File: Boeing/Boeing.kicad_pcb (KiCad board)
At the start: 2 copper layers, 75 x 25 mm, 1 part

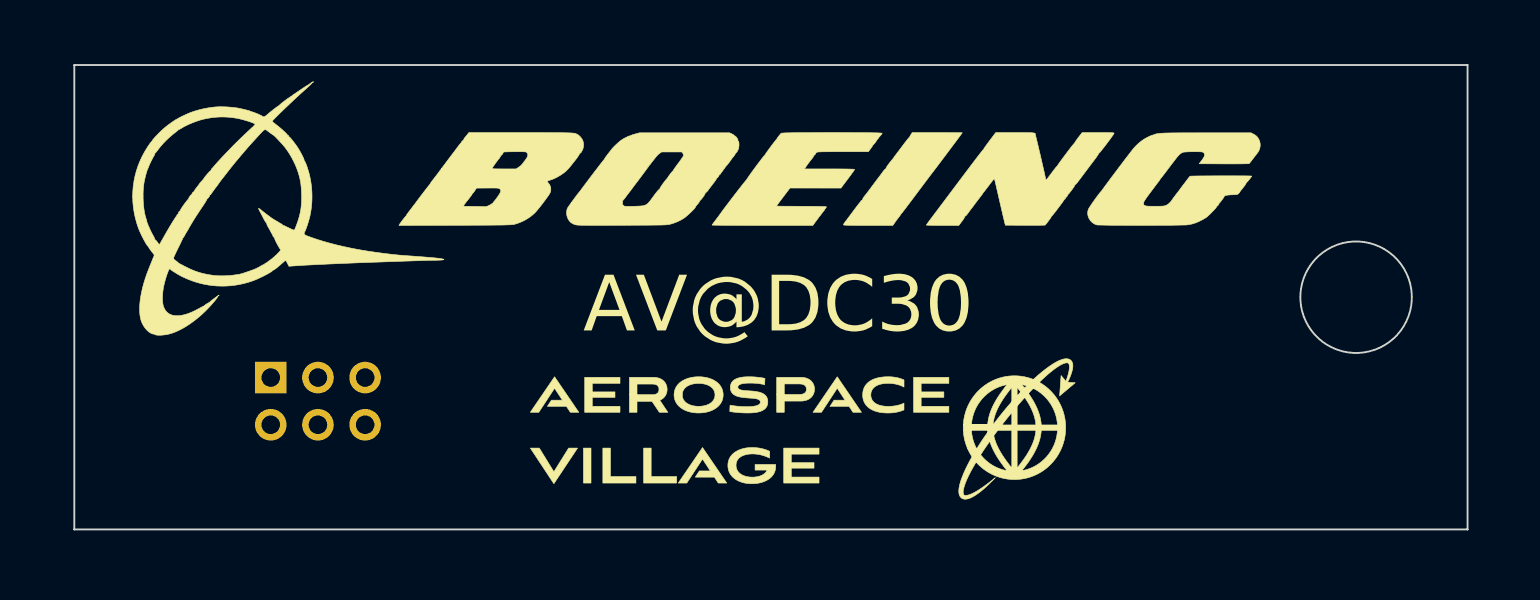
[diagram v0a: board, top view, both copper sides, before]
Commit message: Boeing SAO update to give their logo more space
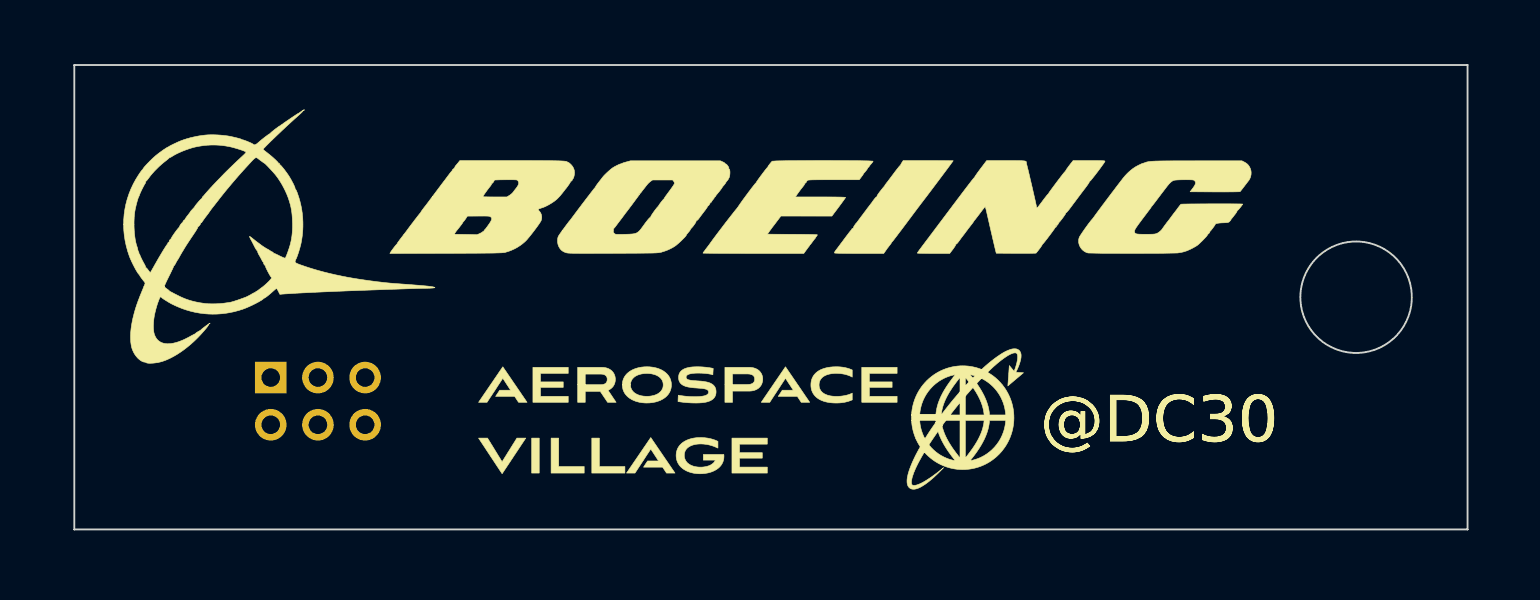
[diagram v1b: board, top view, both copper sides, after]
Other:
- board text added: "@DC30"
- board text removed: "AV@DC30"

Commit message: updated the Boeing SAO to reflect their logo guidelines and added an LED
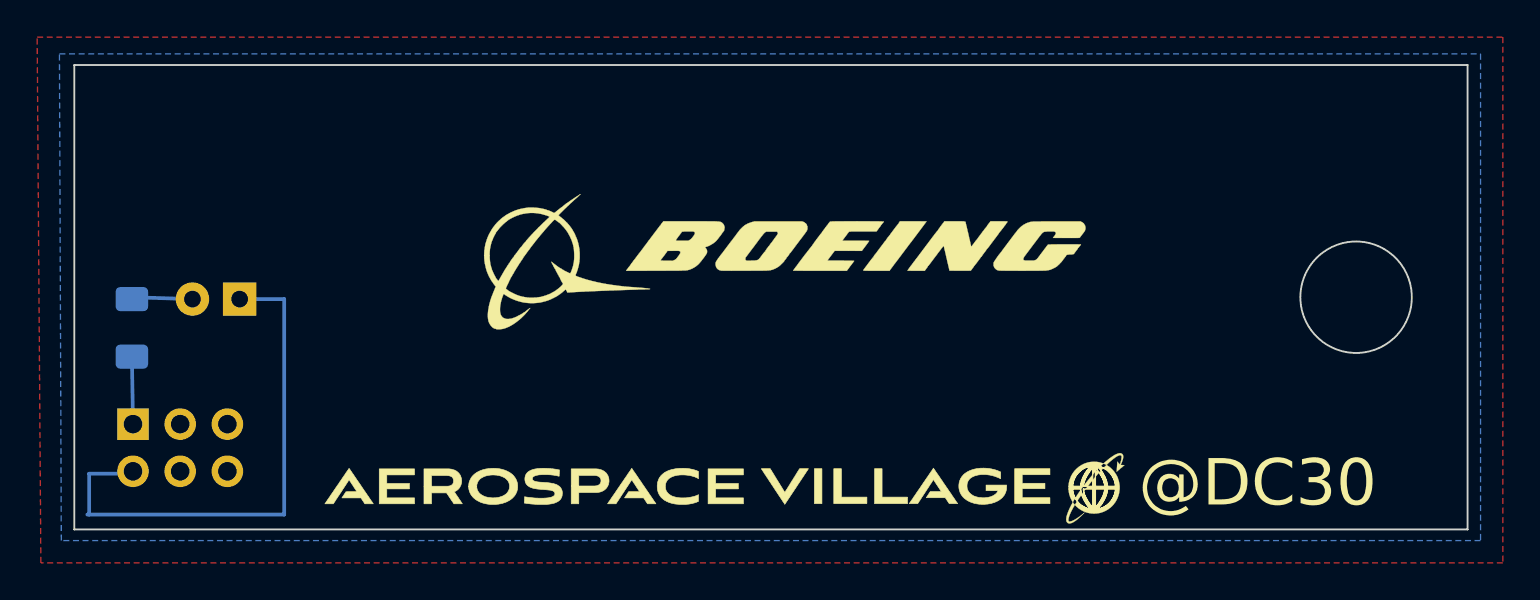
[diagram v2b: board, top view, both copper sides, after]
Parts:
- added REF**: LED_D5.0mm, LED_THT:LED_D5.0mm, F.Cu at (108.9, 62.6)
- added REF**: R_1206_3216Metric_Pad1.30x1.75mm_HandSolder, Resistor_SMD:R_1206_3216Metric_Pad1.30x1.75mm_HandSolder, B.Cu at (103.1, 64.2)
- moved REF** 7.83 mm to (103.2, 69.3)
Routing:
- added copper zone on B.Cu, net (none)
- added copper zone on F.Cu, net (none)
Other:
- board text added: "v3"
- board text removed: "v1"

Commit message: v3 of Boeing SAO
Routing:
- net (no net): track 0.00 -> 32.2 mm
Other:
- board text added: "@av_pubs v3"
- board text removed: "v3"
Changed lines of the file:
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@@
   )
   (setup
+    (stackup
+      (layer "F.SilkS" (type "Top Silk Screen"))
+      (layer "F.Paste" (type "Top Solder Paste"))
+      (layer "F.Mask" (type "Top Solder Mask") (thickness 0.01))
+      (layer "F.Cu" (type "copper") (thickness 0.035))
+      (layer "dielectric 1" (type "core") (thickness 1.51) (material "FR4") (epsilon_r 4.5) (loss_tangent 0.02))
+      (layer "B.Cu" (type "copper") (thickness 0.035))
+      (layer "B.Mask" (type "Bottom Solder Mask") (thickness 0.01))
+      (layer "B.Paste" (type "Bottom Solder Paste"))
+      (layer "B.SilkS" (type "Bottom Silk Screen"))
+      (copper_finish "None")
+      (dielectric_constraints no)
+    )
     (pad_to_mask_clearance 0)
     (pcbplotparams
@@
       (plot_on_all_layers_selection 0x0000000_00000000)
       (disableapertmacros false)
-      (usegerberextensions true)
-      (usegerberattributes true)
+      (usegerberextensions false)
+      (usegerberattributes false)
       (usegerberadvancedattributes false)
       (creategerberjobfile false)
@@
     )
   )
-  (gr_line (start 111.3 74.2) (end 111.3 62.6)
-    (stroke (width 0.2) (type default)) (layer "B.Cu"))
-  (gr_line (start 100.8 72) (end 100.8 74.2)
-    (stroke (width 0.2) (type default)) (layer "B.Cu"))
-  (gr_line (start 103.1 65.7) (end 103.16 69.33)
-    (stroke (width 0.2) (type default)) (layer "B.Cu"))
-  (gr_line (start 100.7 74.2) (end 111.3 74.2)
-    (stroke (width 0.2) (type default)) (layer "B.Cu"))
-  (gr_line (start 111.3 62.6) (end 108.9 62.6)
-    (stroke (width 0.2) (type default)) (layer "B.Cu"))
-  (gr_line (start 100.8 72) (end 103.1 72)
-    (stroke (width 0.2) (type default)) (layer "B.Cu"))
-  (gr_line (start 103.1 62.5) (end 106.3 62.6)
-    (stroke (width 0.2) (type default)) (layer "B.Cu"))
   (gr_line (start 153.74701 72.576395) (end 153.740758 72.626782)
     (stroke (width 0.019843) (type solid)) (layer "F.SilkS"))
@@
   (gr_circle (center 169 62.5) (end 172 62.5)
     (stroke (width 0.1) (type default)) (fill none) (layer "Edge.Cuts"))
-  (gr_text "v3" (at 173.6 74) (layer "B.SilkS")
-    (effects (font (size 1 1) (thickness 0.15)) (justify mirror))
+  (gr_text "@av_pubs\nv3" (at 174.2 55) (layer "B.Cu")
+    (effects (font (size 1.5 1.5) (thickness 0.3) bold) (justify left bottom mirror))
   )
   (gr_text "jlcjlcjlcjlc" (at 173.5 62.6 90) (layer "B.SilkS")
@@
     )
   )
+  (segment (start 103.1 74.2) (end 103.16 74.14) (width 0.254) (layer "B.Cu") (net 0))
+  (segment (start 103.2 74.3) (end 103.1 74.2) (width 0.254) (layer "B.Cu") (net 0))
+  (segment (start 103.16 74.14) (end 103.16 71.87) (width 0.254) (layer "B.Cu") (net 0))
+  (segment (start 113.6 67.3) (end 113.6 72.2) (width 0.254) (layer "B.Cu") (net 0))
+  (segment (start 113.6 72.2) (end 111.5 74.3) (width 0.254) (layer "B.Cu") (net 0))
+  (segment (start 106.36 62.6) (end 103.1 62.6) (width 0.254) (layer "B.Cu") (net 0))
+  (segment (start 103.16 65.76) (end 103.16 69.33) (width 0.254) (layer "B.Cu") (net 0))
+  (segment (start 103.1 65.7) (end 103.16 65.76) (width 0.254) (layer "B.Cu") (net 0))
+  (segment (start 108.9 62.6) (end 113.6 67.3) (width 0.254) (layer "B.Cu") (net 0))
+  (segment (start 111.5 74.3) (end 103.2 74.3) (width 0.254) (layer "B.Cu") (net 0))
   (zone (net 0) (net_name "") (layer "F.Cu") (hatch edge 0.508)
     (connect_pads (clearance 0.508))

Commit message: v4 of Boeing SAO
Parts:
- removed REF**: LED_D5.0mm, LED_THT:LED_D5.0mm
- removed REF**: PinHeader_2x03_P2.54mm_Vertical, Connector_PinHeader_2.54mm:PinHeader_2x03_P2.54mm_Vertical
- removed REF**: R_1206_3216Metric_Pad1.30x1.75mm_HandSolder, Resistor_SMD:R_1206_3216Metric_Pad1.30x1.75mm_HandSolder
- added D1: LED, LED_THT:LED_D5.0mm, F.Cu at (108.9, 62.6)
- added J1: Conn_02x03_Counter_Clockwise, Connector_PinHeader_2.54mm:PinHeader_2x03_P2.54mm_Vertical, B.Cu at (103.2, 69.3)
- added R1: R, Resistor_SMD:R_1206_3216Metric_Pad1.30x1.75mm_HandSolder, B.Cu at (101.7, 62.5)
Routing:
- net (no net): track 32.2 -> 0.00 mm
- net Net-(D1-K): track 0.00 -> 24.1 mm
- net Net-(J1-Pin_1): track 0.00 -> 5.88 mm
- net Net-(D1-A): track 0.00 -> 5.34 mm
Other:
- outline, holes or cut-outs redrawn
- board text added: "@av_pubs v4"
- board text removed: "@av_pubs v3"
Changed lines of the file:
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@@
   )
   (net 0 "")
+  (net 1 "Net-(D1-K)")
+  (net 2 "Net-(D1-A)")
+  (net 3 "Net-(J1-Pin_1)")
+  (net 4 "unconnected-(J1-Pin_3)")
+  (net 5 "unconnected-(J1-Pin_4)")
+  (net 6 "unconnected-(J1-Pin_5)")
+  (net 7 "unconnected-(J1-Pin_6)")
   (footprint "LED_THT:LED_D5.0mm" (layer "F.Cu")
     (at 108.9 62.6 180)
     (descr "LED, diameter 5.0mm, 2 pins, http://cdn-reichelt.de/documents/datenblatt/A500/LL-504BC2E-009.pdf")
     (tags "LED diameter 5.0mm 2 pins")
+    (property "Sheetfile" "File: Boeing.kicad_sch")
+    (property "Sheetname" "")
+    (property "ki_description" "Light emitting diode")
+    (property "ki_keywords" "LED diode")
     (attr through_hole)
-    (fp_text reference "REF**" (at 1.27 -3.96) (layer "F.SilkS") hide
+    (fp_text reference "D1" (at 1.27 -3.96) (layer "F.SilkS") hide
         (effects (font (size 1 1) (thickness 0.15)))
     )
-    (fp_text value "LED_D5.0mm" (at 1.27 3.96) (layer "F.Fab")
+    (fp_text value "LED" (at 1.27 3.96) (layer "F.Fab")
         (effects (font (size 1 1) (thickness 0.15)))
     )
@@
         (effects (font (size 0.8 0.8) (thickness 0.2)))
     )
+    (fp_line (start -1.29 -1.545) (end -1.29 1.545)
+      (stroke (width 0.12) (type solid)) (layer "F.SilkS"))
+    (fp_arc (start -1.29 -1.54483) (mid 2.072002 -2.880433) (end 4.26 0.000462)
+      (stroke (width 0.12) (type solid)) (layer "F.SilkS"))
+    (fp_arc (start 4.26 -0.000462) (mid 2.072002 2.880433) (end -1.29 1.54483)
+      (stroke (width 0.12) (type solid)) (layer "F.SilkS"))
+    (fp_circle (center 1.27 0) (end 3.77 0)
+      (stroke (width 0.12) (type solid)) (fill none) (layer "F.SilkS"))
     (fp_line (start -1.95 -3.25) (end -1.95 3.25)
       (stroke (width 0.05) (type solid)) (layer "F.CrtYd"))
@@
     (fp_circle (center 1.27 0) (end 3.77 0)
       (stroke (width 0.1) (type solid)) (fill none) (layer "F.Fab"))
-    (pad "1" thru_hole rect (at 0 0 180) (size 1.8 1.8) (drill 0.9) (layers *.Cu *.Mask))
-    (pad "2" thru_hole circle (at 2.54 0 180) (size 1.8 1.8) (drill 0.9) (layers *.Cu *.Mask))
+    (pad "1" thru_hole rect (at 0 0 180) (size 1.8 1.8) (drill 0.9) (layers *.Cu *.Mask)
+      (net 1 "Net-(D1-K)") (pinfunction "K") (pintype "passive"))
+    (pad "2" thru_hole circle (at 2.54 0 180) (size 1.8 1.8) (drill 0.9) (layers *.Cu *.Mask)
+      (net 2 "Net-(D1-A)") (pinfunction "A") (pintype "passive"))
     (model "${KICAD6_3DMODEL_DIR}/LED_THT.3dshapes/LED_D5.0mm.wrl"
       (offset (xyz 0 0 0))
@@
     (descr "Through hole straight pin header, 2x03, 2.54mm pitch, double rows")
     (tags "Through hole pin header THT 2x03 2.54mm double row")
+    (property "Sheetfile" "File: Boeing.kicad_sch")
+    (property "Sheetname" "")
+    (property "ki_description" "Generic connector, double row, 02x03, counter clockwise pin numbering scheme (similar to DIP packge numbering), script generated (kicad-library-utils/schlib/autogen/connector/)")
+    (property "ki_keywords" "connector")
     (attr through_hole)
-    (fp_text reference "REF**" (at 1.27 2.33 90) (layer "B.SilkS") hide
+    (fp_text reference "J1" (at 1.27 2.33 90) (layer "B.SilkS") hide
         (effects (font (size 1 1) (thickness 0.15)) (justify mirror))
     )
-    (fp_text value "PinHeader_2x03_P2.54mm_Vertical" (at 5.17 -0.14 -180) (layer "B.Fab")
+    (fp_text value "Conn_02x03_Counter_Clockwise" (at 1.27 -7.41 90) (layer "B.Fab")
         (effects (font (size 1 1) (thickness 0.15)) (justify mirror))
     )
@@
     (fp_line (start 3.81 1.27) (end 3.81 -6.35)
       (stroke (width 0.1) (type solid)) (layer "B.Fab"))
-    (pad "1" thru_hole rect (at 0 0 270) (size 1.7 1.7) (drill 1) (layers *.Cu *.Mask))
-    (pad "2" thru_hole oval (at 2.54 0 270) (size 1.7 1.7) (drill 1) (layers *.Cu *.Mask))
-    (pad "3" thru_hole oval (at 0 -2.54 270) (size 1.7 1.7) (drill 1) (layers *.Cu *.Mask))
-    (pad "4" thru_hole oval (at 2.54 -2.54 270) (size 1.7 1.7) (drill 1) (layers *.Cu *.Mask))
-    (pad "5" thru_hole oval (at 0 -5.08 270) (size 1.7 1.7) (drill 1) (layers *.Cu *.Mask))
-    (pad "6" thru_hole oval (at 2.54 -5.08 270) (size 1.7 1.7) (drill 1) (layers *.Cu *.Mask))
+    (pad "1" thru_hole rect (at 0 0 270) (size 1.7 1.7) (drill 1) (layers *.Cu *.Mask)
+      (net 3 "Net-(J1-Pin_1)") (pinfunction "Pin_1") (pintype "passive"))
+    (pad "2" thru_hole oval (at 2.54 0 270) (size 1.7 1.7) (drill 1) (layers *.Cu *.Mask)
+      (net 1 "Net-(D1-K)") (pinfunction "Pin_2") (pintype "passive"))
+    (pad "3" thru_hole oval (at 0 -2.54 270) (size 1.7 1.7) (drill 1) (layers *.Cu *.Mask)
+      (net 4 "unconnected-(J1-Pin_3)") (pinfunction "Pin_3") (pintype "passive+no_connect"))
+    (pad "4" thru_hole oval (at 2.54 -2.54 270) (size 1.7 1.7) (drill 1) (layers *.Cu *.Mask)
+      (net 5 "unconnected-(J1-Pin_4)") (pinfunction "Pin_4") (pintype "passive+no_connect"))
+    (pad "5" thru_hole oval (at 0 -5.08 270) (size 1.7 1.7) (drill 1) (layers *.Cu *.Mask)
+      (net 6 "unconnected-(J1-Pin_5)") (pinfunction "Pin_5") (pintype "passive+no_connect"))
+    (pad "6" thru_hole oval (at 2.54 -5.08 270) (size 1.7 1.7) (drill 1) (layers *.Cu *.Mask)
+      (net 7 "unconnected-(J1-Pin_6)") (pinfunction "Pin_6") (pintype "passive+no_connect"))
     (model "${KICAD6_3DMODEL_DIR}/Connector_PinHeader_2.54mm.3dshapes/PinHeader_2x03_P2.54mm_Vertical.wrl"
       (offset (xyz 0 0 0))
@@
   )
   (footprint "Resistor_SMD:R_1206_3216Metric_Pad1.30x1.75mm_HandSolder" (layer "B.Cu")
-    (at 103.1 64.15 -90)
+    (at 101.7 62.5 -90)
     (descr "Resistor SMD 1206 (3216 Metric), square (rectangular) end terminal, IPC_7351 nominal with elongated pad for handsoldering. (Body size source: IPC-SM-782 page 72, https://www.pcb-3d.com/wordpress/wp-content/uploads/ipc-sm-782a_amendment_1_and_2.pdf), generated with kicad-footprint-generator")
     (tags "resistor handsolder")
+    (property "Sheetfile" "File: Boeing.kicad_sch")
+    (property "Sheetname" "")
+    (property "ki_description" "Resistor")
+    (property "ki_keywords" "R res resistor")
     (attr smd)
-    (fp_text reference "REF**" (at 0 1.82 -270) (layer "B.SilkS") hide
+    (fp_text reference "R1" (at 0 1.82 90) (layer "B.SilkS") hide
         (effects (font (size 1 1) (thickness 0.15)) (justify mirror))
     )
-    (fp_text value "R_1206_3216Metric_Pad1.30x1.75mm_HandSolder" (at 0.05 2 -270) (layer "B.Fab")
+    (fp_text value "R" (at 0 -1.82 90) (layer "B.Fab")
         (effects (font (size 1 1) (thickness 0.15)) (justify mirror))
     )
-    (fp_text user "${REFERENCE}" (at 0 0 -270) (layer "B.Fab")
+    (fp_text user "${REFERENCE}" (at 0 0 90) (layer "B.Fab")
         (effects (font (size 0.8 0.8) (thickness 0.12)) (justify mirror))
     )
@@
     (fp_line (start 1.6 0.8) (end 1.6 -0.8)
       (stroke (width 0.1) (type solid)) (layer "B.Fab"))
-    (pad "1" smd roundrect (at -1.55 0 270) (size 1.3 1.75) (layers "B.Cu" "B.Paste" "B.Mask") (roundrect_rratio 0.1923076923))
-    (pad "2" smd roundrect (at 1.55 0 270) (size 1.3 1.75) (layers "B.Cu" "B.Paste" "B.Mask") (roundrect_rratio 0.1923076923))
+    (pad "1" smd roundrect (at -1.55 0 270) (size 1.3 1.75) (layers "B.Cu" "B.Paste" "B.Mask") (roundrect_rratio 0.1923076923)
+      (net 2 "Net-(D1-A)") (pintype "passive"))
+    (pad "2" smd roundrect (at 1.55 0 270) (size 1.3 1.75) (layers "B.Cu" "B.Paste" "B.Mask") (roundrect_rratio 0.1923076923)
+      (net 3 "Net-(J1-Pin_1)") (pintype "passive"))
     (model "${KICAD6_3DMODEL_DIR}/Resistor_SMD.3dshapes/R_1206_3216Metric.wrl"
       (offset (xyz 0 0 0))
@@
   (gr_rect (start 100 50) (end 175 75)
     (stroke (width 0.1) (type default)) (fill none) (layer "Edge.Cuts"))
-  (gr_circle (center 169 62.5) (end 172 62.5)
-    (stroke (width 0.1) (type default)) (fill none) (layer "Edge.Cuts"))
-  (gr_text "@av_pubs\nv3" (at 174.2 55) (layer "B.Cu")
+  (gr_text "@av_pubs\nv4" (at 174.2 55) (layer "B.Cu")
     (effects (font (size 1.5 1.5) (thickness 0.3) bold) (justify left bottom mirror))
   )
@@
     )
   )
-  (segment (start 103.1 74.2) (end 103.16 74.14) (width 0.254) (layer "B.Cu") (net 0))
-  (segment (start 103.2 74.3) (end 103.1 74.2) (width 0.254) (layer "B.Cu") (net 0))
-  (segment (start 103.16 74.14) (end 103.16 71.87) (width 0.254) (layer "B.Cu") (net 0))
-  (segment (start 113.6 67.3) (end 113.6 72.2) (width 0.254) (layer "B.Cu") (net 0))
-  (segment (start 113.6 72.2) (end 111.5 74.3) (width 0.254) (layer "B.Cu") (net 0))
-  (segment (start 106.36 62.6) (end 103.1 62.6) (width 0.254) (layer "B.Cu") (net 0))
-  (segment (start 103.16 65.76) (end 103.16 69.33) (width 0.254) (layer "B.Cu") (net 0))
-  (segment (start 103.1 65.7) (end 103.16 65.76) (width 0.254) (layer "B.Cu") (net 0))
-  (segment (start 108.9 62.6) (end 113.6 67.3) (width 0.254) (layer "B.Cu") (net 0))
-  (segment (start 111.5 74.3) (end 103.2 74.3) (width 0.254) (layer "B.Cu") (net 0))
+  (segment (start 112.7 72.8) (end 111.1 74.4) (width 0.25) (layer "B.Cu") (net 1))
+  (segment (start 111.1 74.4) (end 105.69 74.4) (width 0.25) (layer "B.Cu") (net 1))
+  (segment (start 110.8 62.6) (end 112.7 64.5) (width 0.25) (layer "B.Cu") (net 1))
+  (segment (start 108.9 62.6) (end 110.8 62.6) (width 0.25) (layer "B.Cu") (net 1))
+  (segment (start 112.7 64.5) (end 112.7 72.8) (width 0.25) (layer "B.Cu") (net 1))
+  (segment (start 105.69 74.4) (end 103.16 71.87) (width 0.25) (layer "B.Cu") (net 1))
+  (segment (start 104.71 60.95) (end 106.36 62.6) (width 0.25) (layer "B.Cu") (net 2))
+  (segment (start 101.7 60.95) (end 104.71 60.95) (width 0.25) (layer "B.Cu") (net 2))
+  (segment (start 103.16 69.33) (end 103.16 65.51) (width 0.25) (layer "B.Cu") (net 3))
+  (segment (start 103.16 65.51) (end 101.7 64.05) (width 0.25) (layer "B.Cu") (net 3))
   (zone (net 0) (net_name "") (layer "F.Cu") (hatch edge 0.508)
     (connect_pads (clearance 0.508))
